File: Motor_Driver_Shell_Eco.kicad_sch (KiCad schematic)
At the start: 0 parts

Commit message: SCHEMATIC DONE - NEED REVIEW
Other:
- added sheet HALL_INPUT (hall_input.kicad_sch)
- added sheet UTILITY (utility.kicad_sch)
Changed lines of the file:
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@@
 	(paper "A4")
 	(sheet
-		(at 44.45 46.99)
-		(size 30.48 15.24)
+		(at 41.91 68.58)
+		(size 41.91 17.78)
+		(exclude_from_sim no)
+		(in_bom yes)
+		(on_board yes)
+		(dnp no)
+		(fields_autoplaced yes)
+		(stroke
+			(width 0.1524)
+			(type solid)
+		)
+		(fill
+			(color 0 0 0 0.0000)
+		)
+		(property "Sheetname" "UTILITY"
+			(at 41.91 67.8684 0)
+			(effects
+				(font
+					(size 1.27 1.27)
+				)
+				(justify left bottom)
+			)
+		)
+		(property "Sheetfile" "utility.kicad_sch"
+			(at 41.91 86.9446 0)
+			(effects
+				(font
+					(size 1.27 1.27)
+				)
+				(justify left top)
+			)
+		)
+		(property "Field2" ""
+			(at 41.91 68.58 0)
+			(effects
+				(font
+					(size 1.27 1.27)
+				)
+			)
+		)
+		(instances
+			(project "Motor_Driver_Shell_Eco"
+				(path "/63ef3b9c-05f1-4b00-812a-fede2372efc7"
+					(page "6")
+				)
+			)
+		)
+	)
+	(sheet
+		(at 41.91 46.99)
+		(size 43.18 15.24)
 		(exclude_from_sim no)
 		(in_bom yes)
@@
 		)
 		(property "Sheetname" "V_IN"
-			(at 44.45 46.2784 0)
+			(at 41.91 46.2784 0)
 			(effects
 				(font
@@
 		)
 		(property "Sheetfile" "vin.kicad_sch"
-			(at 44.45 62.8146 0)
+			(at 41.91 62.8146 0)
 			(effects
 				(font
@@
 		)
 		(property "Field2" ""
-			(at 44.45 46.99 0)
+			(at 41.91 46.99 0)
 			(effects
 				(font
@@
 				)
 			)
+		)
+	)
+	(sheet
+		(at 40.64 92.71)
+		(size 43.18 11.43)
+		(exclude_from_sim no)
+		(in_bom yes)
+		(on_board yes)
+		(dnp no)
+		(fields_autoplaced yes)
+		(stroke
+			(width 0.1524)
+			(type solid)
+		)
+		(fill
+			(color 0 0 0 0.0000)
+		)
+		(property "Sheetname" "HALL_INPUT"
+			(at 40.64 91.9984 0)
+			(effects
+				(font
+					(size 1.27 1.27)
+				)
+				(justify left bottom)
+			)
+		)
+		(property "Sheetfile" "hall_input.kicad_sch"
+			(at 40.64 104.7246 0)
+			(effects
+				(font
+					(size 1.27 1.27)
+				)
+				(justify left top)
+			)
+		)
+		(instances
+			(project "Motor_Driver_Shell_Eco"
+				(path "/63ef3b9c-05f1-4b00-812a-fede2372efc7"
+					(page "5")
+				)
+			)

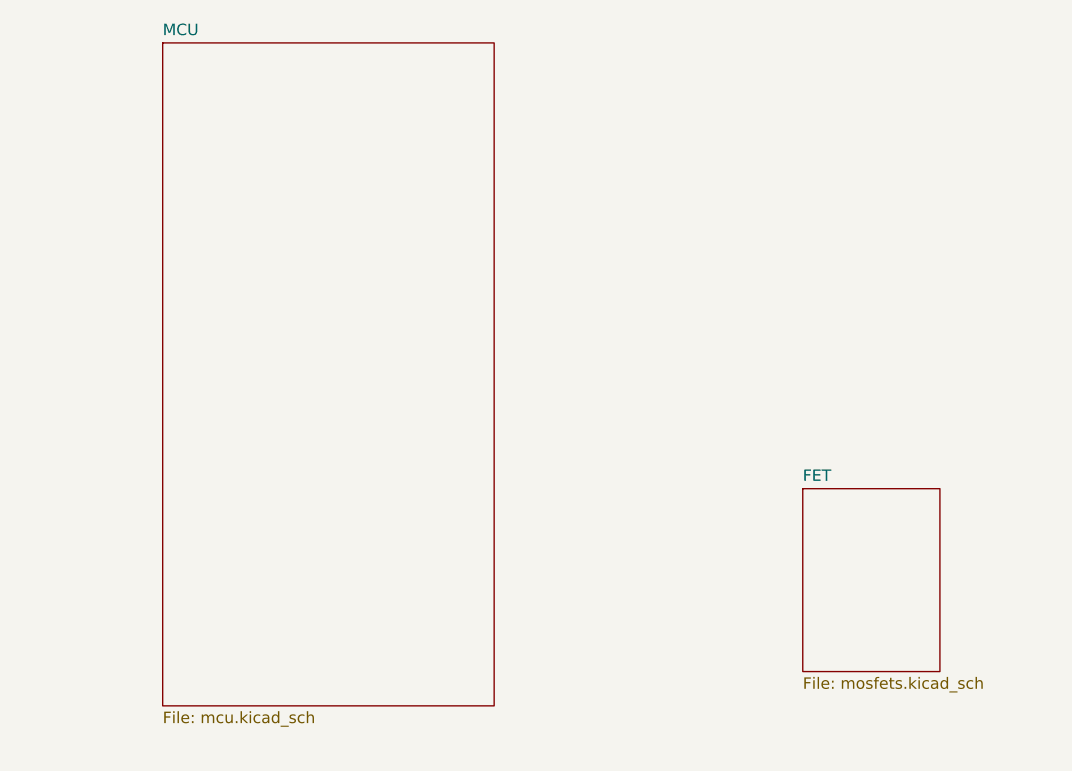
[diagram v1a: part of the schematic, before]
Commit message: update: revised label
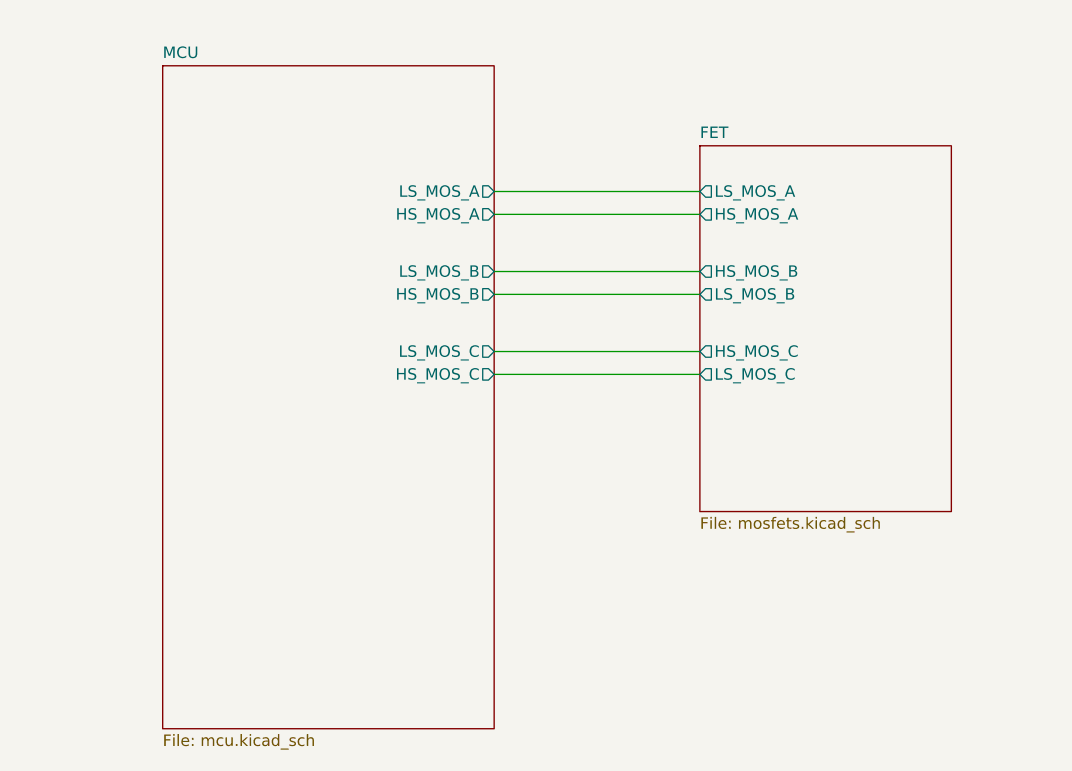
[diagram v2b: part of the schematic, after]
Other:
- sheet FET ports: added HS_MOS_A, HS_MOS_B, HS_MOS_C, LS_MOS_A, LS_MOS_B, LS_MOS_C; removed none
- sheet MCU ports: added HS_MOS_A, HS_MOS_B, HS_MOS_C, LS_MOS_A, LS_MOS_B, LS_MOS_C; removed none
- title: (none) -> MDU
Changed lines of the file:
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@@
 	(generator_version "9.0")
 	(paper "A4")
+	(title_block
+		(title "MDU")
+		(date "2025-12-20")
+		(rev "0.01")
+	)
+	(wire
+		(pts
+			(xy 147.32 62.23) (xy 170.18 62.23)
+		)
+		(stroke
+			(width 0)
+			(type default)
+		)
+	)
+	(wire
+		(pts
+			(xy 147.32 71.12) (xy 170.18 71.12)
+		)
+		(stroke
+			(width 0)
+			(type default)
+		)
+	)
+	(wire
+		(pts
+			(xy 147.32 77.47) (xy 170.18 77.47)
+		)
+		(stroke
+			(width 0)
+			(type default)
+		)
+	)
+	(wire
+		(pts
+			(xy 147.32 68.58) (xy 170.18 68.58)
+		)
+		(stroke
+			(width 0)
+			(type default)
+		)
+	)
+	(wire
+		(pts
+			(xy 147.32 80.01) (xy 170.18 80.01)
+		)
+		(stroke
+			(width 0)
+			(type default)
+		)
+	)
+	(wire
+		(pts
+			(xy 147.32 59.69) (xy 170.18 59.69)
+		)
+		(stroke
+			(width 0)
+			(type default)
+		)
+	)
 	(sheet
 		(at 41.91 68.58)
@@
 	)
 	(sheet
-		(at 181.61 92.71)
-		(size 15.24 20.32)
+		(at 170.18 54.61)
+		(size 27.94 40.64)
 		(exclude_from_sim no)
 		(in_bom yes)
@@
 		)
 		(property "Sheetname" "FET"
-			(at 181.61 91.9984 0)
+			(at 170.18 53.8984 0)
 			(effects
 				(font
@@
 		)
 		(property "Sheetfile" "mosfets.kicad_sch"
-			(at 181.61 113.6146 0)
-			(effects
-				(font
-					(size 1.27 1.27)
-				)
-				(justify left top)
+			(at 170.18 95.8346 0)
+			(effects
+				(font
+					(size 1.27 1.27)
+				)
+				(justify left top)
+			)
+		)
+		(pin "HS_MOS_A" output
+			(at 170.18 62.23 180)
+			(effects
+				(font
+					(size 1.27 1.27)
+				)
+				(justify left)
+			)
+		)
+		(pin "HS_MOS_B" output
+			(at 170.18 68.58 180)
+			(effects
+				(font
+					(size 1.27 1.27)
+				)
+				(justify left)
+			)
+		)
+		(pin "HS_MOS_C" output
+			(at 170.18 77.47 180)
+			(effects
+				(font
+					(size 1.27 1.27)
+				)
+				(justify left)
+			)
+		)
+		(pin "LS_MOS_A" output
+			(at 170.18 59.69 180)
+			(effects
+				(font
+					(size 1.27 1.27)
+				)
+				(justify left)
+			)
+		)
+		(pin "LS_MOS_B" output
+			(at 170.18 71.12 180)
+			(effects
+				(font
+					(size 1.27 1.27)
+				)
+				(justify left)
+			)
+		)
+		(pin "LS_MOS_C" output
+			(at 170.18 80.01 180)
+			(effects
+				(font
+					(size 1.27 1.27)
+				)
+				(justify left)
 			)
 		)
@@
 	)
 	(sheet
-		(at 110.49 43.18)
+		(at 110.49 45.72)
 		(size 36.83 73.66)
 		(exclude_from_sim no)
@@
 		)
 		(property "Sheetname" "MCU"
-			(at 110.49 42.4684 0)
+			(at 110.49 45.0084 0)
 			(effects
 				(font
@@
 		)
 		(property "Sheetfile" "mcu.kicad_sch"
-			(at 110.49 117.4246 0)
-			(effects
-				(font
-					(size 1.27 1.27)
-				)
-				(justify left top)
-			)
-		)
+			(at 110.49 119.9646 0)
+			(effects
+				(font
+					(size 1.27 1.27)
+				)
+				(justify left top)
+			)
+		)
+		(pin "HS_MOS_B" output
+			(at 147.32 71.12 0)
+			(effects
+				(font
+					(size 1.27 1.27)
+				)
+				(justify right)
+			)
+		)
+		(pin "HS_MOS_C" output
+			(at 147.32 80.01 0)
+			(effects
+				(font
+					(size 1.27 1.27)
+				)
+				(justify right)
+			)
+		)
+		(pin "LS_MOS_C" output
+			(at 147.32 77.47 0)
+			(effects
+				(font
+					(size 1.27 1.27)
+				)
+				(justify right)
+			)
+		)
+		(pin "LS_MOS_A" output
+			(at 147.32 59.69 0)
+			(effects
+				(font
+					(size 1.27 1.27)
+				)
+				(justify right)
+			)
+		)
+		(pin "HS_MOS_A" output
+			(at 147.32 62.23 0)
+			(effects
+				(font
+					(size 1.27 1.27)
+				)
+				(justify right)
+			)
+		)
+		(pin "LS_MOS_B" output
+			(at 147.32 68.58 0)
+			(effects
+				(font
+					(size 1.27 1.27)
+				)
+				(justify right)
+			)
+		)

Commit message: bit artık
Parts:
- added H10, H3, H8, H9: MountingHole, MountingHole:MountingHole_2.2mm_M2, symbol Mechanical:MountingHole

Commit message: rev3
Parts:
- added H4, H6: MountingHole, MountingHole:MountingHole_2.2mm_M2, symbol Mechanical:MountingHole
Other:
- moved on the sheet: H10, H3, H8, H9
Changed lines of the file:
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@@
+	(wire
+		(pts
+			(xy 147.32 68.58) (xy 170.18 68.58)
+		)
+		(stroke
+			(width 0)
+			(type default)
+		)
+	)
+	(wire
+		(pts
+			(xy 147.32 77.47) (xy 170.18 77.47)
+		)
+		(stroke
+			(width 0)
+			(type default)
+		)
+	)
+	(wire
+		(pts
+			(xy 147.32 80.01) (xy 170.18 80.01)
+		)
+		(stroke
+			(width 0)
+			(type default)
+		)
+	)
+	(wire
+		(pts
+			(xy 147.32 59.69) (xy 170.18 59.69)
+		)
+		(stroke
+			(width 0)
+			(type default)
+		)
+	)
 	(wire
 		(pts
@@
 		)
 	)
-	(wire
-		(pts
-			(xy 147.32 77.47) (xy 170.18 77.47)
-		)
-		(stroke
-			(width 0)
-			(type default)
-		)
-	)
-	(wire
-		(pts
-			(xy 147.32 68.58) (xy 170.18 68.58)
-		)
-		(stroke
-			(width 0)
-			(type default)
-		)
-	)
-	(wire
-		(pts
-			(xy 147.32 80.01) (xy 170.18 80.01)
-		)
-		(stroke
-			(width 0)
-			(type default)
-		)
-	)
-	(wire
-		(pts
-			(xy 147.32 59.69) (xy 170.18 59.69)
-		)
-		(stroke
-			(width 0)
-			(type default)
-		)
-	)
 	(symbol
 		(lib_id "Mechanical:MountingHole")
-		(at 203.2 157.48 0)
+		(at 180.34 144.78 0)
 		(unit 1)
 		(exclude_from_sim no)
@@
 		(fields_autoplaced yes)
 		(property "Reference" "H8"
-			(at 205.74 156.2099 0)
+			(at 182.88 143.5099 0)
 			(effects
 				(font
@@
 		)
 		(property "Value" "MountingHole"
-			(at 205.74 158.7499 0)
+			(at 182.88 146.0499 0)
 			(effects
 				(font
@@
 		)
 		(property "Footprint" "MountingHole:MountingHole_2.2mm_M2"
-			(at 203.2 157.48 0)
+			(at 180.34 144.78 0)
 			(effects
 				(font
@@
 		)
 		(property "Datasheet" "~"
-			(at 203.2 157.48 0)
+			(at 180.34 144.78 0)
 			(effects
 				(font
@@
 		)
 		(property "Description" "Mounting Hole without connection"
-			(at 203.2 157.48 0)
+			(at 180.34 144.78 0)
 			(effects
 				(font
@@
 	(symbol
 		(lib_id "Mechanical:MountingHole")
-		(at 197.3937 157.451 0)
+		(at 179.6137 152.371 0)
 		(unit 1)
 		(exclude_from_sim no)
@@
 		(fields_autoplaced yes)
 		(property "Reference" "H9"
-			(at 199.9337 156.1809 0)
+			(at 182.1537 151.1009 0)
 			(effects
 				(font
@@
 		)
 		(property "Value" "MountingHole"
-			(at 199.9337 158.7209 0)
+			(at 182.1537 153.6409 0)
 			(effects
 				(font
@@
 		)
 		(property "Footprint" "MountingHole:MountingHole_2.2mm_M2"
-			(at 197.3937 157.451 0)
+			(at 179.6137 152.371 0)
 			(effects
 				(font
@@
 		)
 		(property "Datasheet" "~"
-			(at 197.3937 157.451 0)
+			(at 179.6137 152.371 0)
 			(effects
 				(font
@@
 		)
 		(property "Description" "Mounting Hole without connection"
-			(at 197.3937 157.451 0)
+			(at 179.6137 152.371 0)
 			(effects
 				(font
@@
 	(symbol
 		(lib_id "Mechanical:MountingHole")
-		(at 212.09 157.48 0)
+		(at 180.34 137.16 0)
 		(unit 1)
 		(exclude_from_sim no)
@@
 		(fields_autoplaced yes)
 		(property "Reference" "H3"
-			(at 214.63 156.2099 0)
+			(at 182.88 135.8899 0)
 			(effects
 				(font
@@
 		)
 		(property "Value" "MountingHole"
-			(at 214.63 158.7499 0)
+			(at 182.88 138.4299 0)
 			(effects
 				(font
@@
 		)
 		(property "Footprint" "MountingHole:MountingHole_2.2mm_M2"
-			(at 212.09 157.48 0)
+			(at 180.34 137.16 0)
 			(effects
 				(font
@@
 		)
 		(property "Datasheet" "~"
-			(at 212.09 157.48 0)
+			(at 180.34 137.16 0)
 			(effects
 				(font
@@
 		)
 		(property "Description" "Mounting Hole without connection"
-			(at 212.09 157.48 0)
+			(at 180.34 137.16 0)
 			(effects
 				(font
@@
 	(symbol
 		(lib_id "Mechanical:MountingHole")
-		(at 187.1417 158.9307 0)
+		(at 180.34 121.92 0)
 		(unit 1)
 		(exclude_from_sim no)
@@
 		(dnp no)
 		(fields_autoplaced yes)
+		(property "Reference" "H6"
+			(at 182.88 120.6499 0)
+			(effects
+				(font
+					(size 1.27 1.27)
+				)
+				(justify left)
+			)
+		)
+		(property "Value" "MountingHole"
+			(at 182.88 123.1899 0)
+			(effects
+				(font
+					(size 1.27 1.27)
+				)
+				(justify left)
+			)
+		)
+		(property "Footprint" "MountingHole:MountingHole_2.2mm_M2"
+			(at 180.34 121.92 0)
+			(effects
+				(font
+					(size 1.27 1.27)
+				)
+				(hide yes)
+			)
+		)
+		(property "Datasheet" "~"
+			(at 180.34 121.92 0)
+			(effects
+				(font
+					(size 1.27 1.27)
+				)
+				(hide yes)
+			)
+		)
+		(property "Description" "Mounting Hole without connection"
+			(at 180.34 121.92 0)
+			(effects
+				(font
+					(size 1.27 1.27)
+				)
+				(hide yes)
+			)
+		)
+		(instances
+			(project "Motor_Driver_Shell_Eco"
+				(path "/63ef3b9c-05f1-4b00-812a-fede2372efc7"
+					(reference "H6")
+					(unit 1)
+				)
+			)
+		)
+	)
+	(symbol
+		(lib_id "Mechanical:MountingHole")
+		(at 179.07 160.02 0)
+		(unit 1)
+		(exclude_from_sim no)
+		(in_bom no)
+		(on_board yes)
+		(dnp no)
+		(fields_autoplaced yes)
 		(property "Reference" "H10"
-			(at 189.6817 157.6606 0)
+			(at 181.61 158.7499 0)
 			(effects
 				(font
@@
 		)
 		(property "Value" "MountingHole"
-			(at 189.6817 160.2006 0)
+			(at 181.61 161.2899 0)
 			(effects
 				(font
@@
 		)
 		(property "Footprint" "MountingHole:MountingHole_2.2mm_M2"
-			(at 187.1417 158.9307 0)
+			(at 179.07 160.02 0)
 			(effects
 				(font
@@
 		)
 		(property "Datasheet" "~"
-			(at 187.1417 158.9307 0)
+			(at 179.07 160.02 0)
 			(effects
 				(font
@@
 		)
 		(property "Description" "Mounting Hole without connection"
-			(at 187.1417 158.9307 0)
+			(at 179.07 160.02 0)
 			(effects
 				(font
@@
 				(path "/63ef3b9c-05f1-4b00-812a-fede2372efc7"
 					(reference "H10")
+					(unit 1)
+				)
+			)
+		)
+	)
+	(symbol
+		(lib_id "Mechanical:MountingHole")
+		(at 180.34 129.54 0)
+		(unit 1)
+		(exclude_from_sim no)
+		(in_bom no)
+		(on_board yes)
+		(dnp no)
+		(fields_autoplaced yes)
+		(property "Reference" "H4"
+			(at 182.88 128.2699 0)
+			(effects
+				(font
+					(size 1.27 1.27)
+				)
+				(justify left)
+			)
+		)
+		(property "Value" "MountingHole"
+			(at 182.88 130.8099 0)
+			(effects
+				(font
+					(size 1.27 1.27)
+				)
+				(justify left)
+			)
+		)
+		(property "Footprint" "MountingHole:MountingHole_2.2mm_M2"
+			(at 180.34 129.54 0)
+			(effects
+				(font
+					(size 1.27 1.27)
+				)
+				(hide yes)
+			)
+		)
+		(property "Datasheet" "~"
+			(at 180.34 129.54 0)
+			(effects
+				(font
+					(size 1.27 1.27)
+				)
+				(hide yes)
+			)
+		)
+		(property "Description" "Mounting Hole without connection"
+			(at 180.34 129.54 0)
+			(effects
+				(font
+					(size 1.27 1.27)
+				)
+				(hide yes)
+			)
+		)
+		(instances
+			(project "Motor_Driver_Shell_Eco"
+				(path "/63ef3b9c-05f1-4b00-812a-fede2372efc7"
+					(reference "H4")
 					(unit 1)
 				)
@@
 		)
 		(pin "HS_MOS_B" output
-			(at 170.18 68.58 180)
+			(at 170.18 71.12 180)
 			(effects
 				(font
@@
 		)
 		(pin "HS_MOS_C" output
-			(at 170.18 77.47 180)
+			(at 170.18 80.01 180)
 			(effects
 				(font
@@
 		)
 		(pin "LS_MOS_B" output
-			(at 170.18 71.12 180)
+			(at 170.18 68.58 180)
 			(effects
 				(font
@@
 		)
 		(pin "LS_MOS_C" output
-			(at 170.18 80.01 180)
-			(effects
-				(font
+			(at 170.18 77.47 180)
+			(effects
+				(font
